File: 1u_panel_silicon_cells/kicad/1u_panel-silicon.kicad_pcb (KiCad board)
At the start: 2 copper layers, 83 x 100 mm, 148 parts, among them J1 MMS-104-01-[F/L]-SH, J2 2-1734592-0, Q1 DMP3050LVT-7, Q2 DMP2240UDM-7, U1 TCAN330GDCNT, U10 TPS63060DSCR, U11 TMP101NA/3KSLOTTED, U12 LTC4412, U13 LTC4411, U14 LTC4411, U15 LTC4411, U16 LTC4411, U2 TMP101NA/3KSLOTTED, U3 LT1618EMSTRPBF, U4 INA226, U5 LTC4411, U6 LTC4411, U7 STM32F091CCT7, U8 LTC4411, U9 LTC4411, X1 ECS-160-10-36Q-ES-TR

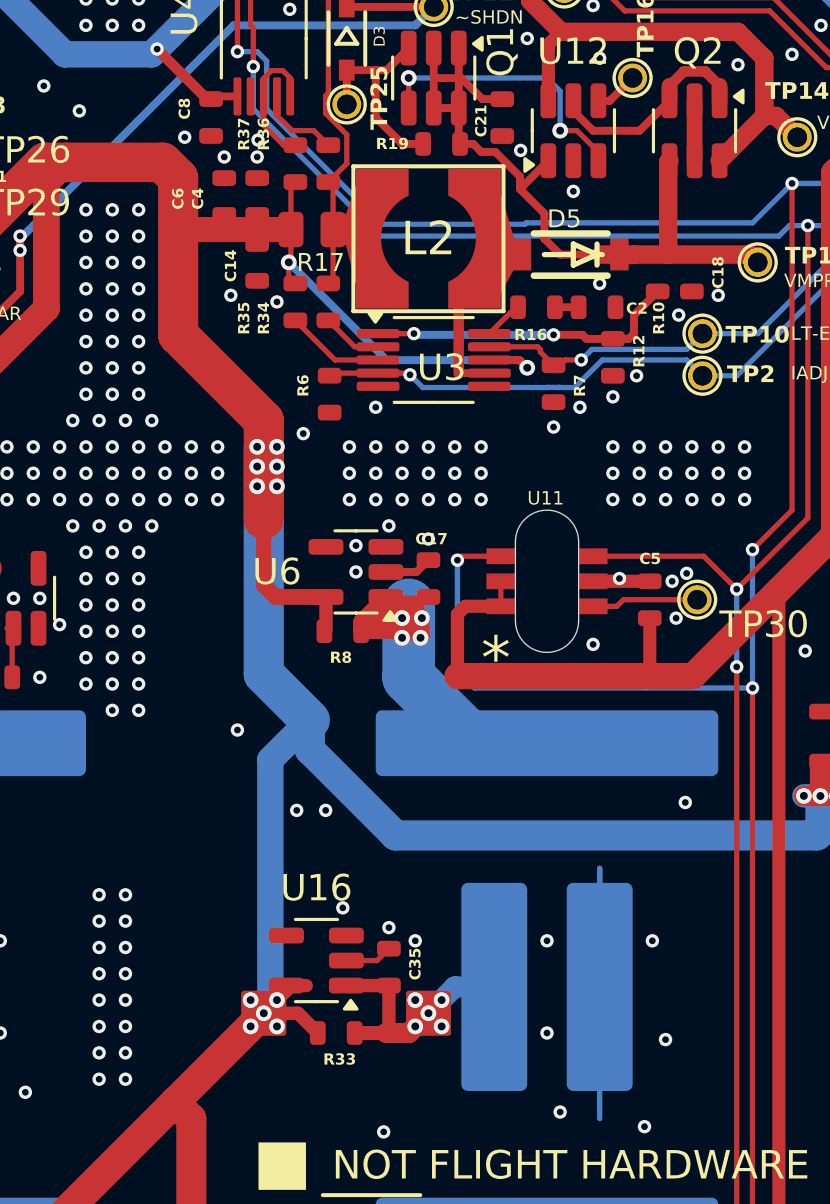
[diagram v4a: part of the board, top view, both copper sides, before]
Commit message: Updated all PN/DS/DPN/MPN/etc. for silicon solar module components
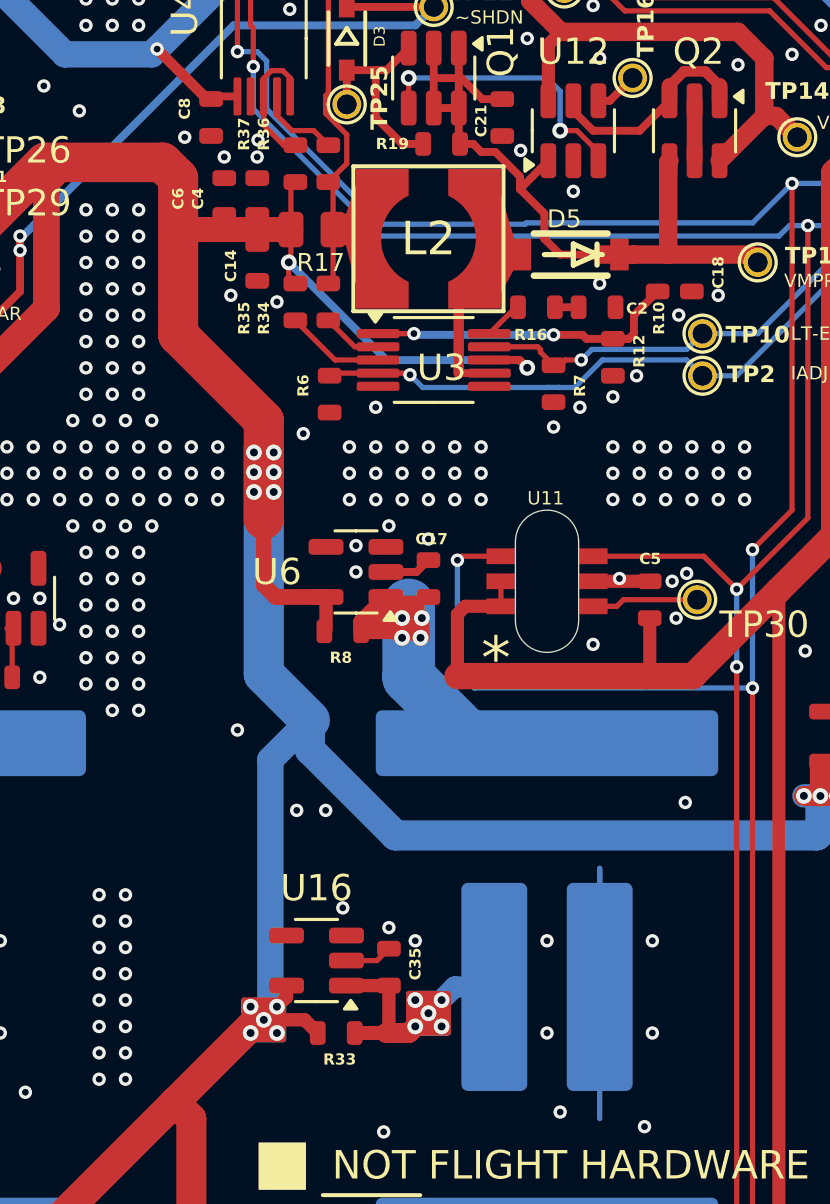
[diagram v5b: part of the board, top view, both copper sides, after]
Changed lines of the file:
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@@
 	)
 	(gr_rect
-		(start 137 105.25)
-		(end 138.5 106.75)
+		(start 137 105.5)
+		(end 138.5 107)
 		(stroke
 			(width 0.2)
@@
 	)
 	(gr_rect
-		(start 137 105.25)
-		(end 138.5 106.75)
+		(start 137 105.5)
+		(end 138.5 107)
 		(stroke
 			(width 0.2)
@@
 	)
 	(segment
-		(start 139.3625 104.95)
-		(end 138.8 104.95)
-		(width 0.508)
-		(layer "F.Cu")
-		(net 2)
-	)
-	(segment
 		(start 135 110)
 		(end 134.375 109.375)
@@
 	)
 	(segment
+		(start 134.5 80.25)
+		(end 137.75 83.5)
+		(width 1.524)
+		(layer "F.Cu")
+		(net 2)
+	)
+	(segment
 		(start 129.287611 114.462389)
 		(end 129.287611 117.962389)
@@
 	)
 	(segment
-		(start 134.5 80.25)
-		(end 137.75 83.5)
-		(width 1.524)
+		(start 138.6125 104.95)
+		(end 138.6125 105.3875)
+		(width 0.508)
 		(layer "F.Cu")
 		(net 2)
 	)
 	(segment
-		(start 137.75 106)
-		(end 139.05 106)
+		(start 174.125 103.375)
+		(end 174.125 101.5)
 		(width 0.508)
 		(layer "F.Cu")
@@
 	)
 	(segment
-		(start 174.125 103.375)
-		(end 174.125 101.5)
+		(start 139.3 106.25)
+		(end 139.8 106.75)
 		(width 0.508)
 		(layer "F.Cu")
@@
 	)
 	(segment
-		(start 134.5 76)
-		(end 134.5 80.25)
+		(start 133.9011 73.7036)
+		(end 134.5 74.3025)
+		(width 1.524)
+		(layer "F.Cu")
+		(net 2)
+	)
+	(segment
+		(start 137.75 83.5)
+		(end 137.75 87.25)
 		(width 1.524)
 		(layer "F.Cu")
@@
 	)
 	(segment
-		(start 137.75 83.5)
-		(end 137.75 87.25)
-		(width 1.524)
+		(start 158.25 97.75)
+		(end 159.8 97.75)
+		(width 0.762)
 		(layer "F.Cu")
 		(net 2)
 	)
 	(segment
-		(start 158.25 97.75)
-		(end 159.8 97.75)
-		(width 0.762)
+		(start 134.5 74.3025)
+		(end 134.5 80.25)
+		(width 1.524)
 		(layer "F.Cu")
 		(net 2)
@@
 	)
 	(segment
-		(start 134.5 74.3025)
-		(end 134.5 76)
-		(width 1.524)
-		(layer "F.Cu")
-		(net 2)
-	)
-	(segment
 		(start 138.6125 121.6125)
 		(end 135 118)
@@
 	)
 	(segment
-		(start 139.05 106)
-		(end 139.8 106.75)
-		(width 0.508)
-		(layer "F.Cu")
-		(net 2)
-	)
-	(segment
 		(start 134.753898 76.253898)
 		(end 138.780425 76.253898)
@@
 	)
 	(segment
-		(start 138.8 104.95)
-		(end 137.75 106)
-		(width 0.508)
-		(layer "F.Cu")
-		(net 2)
-	)
-	(segment
 		(start 138.780425 76.253898)
 		(end 138.780425 77.418475)
@@
 	)
 	(segment
+		(start 138.6125 105.3875)
+		(end 137.75 106.25)
+		(width 0.508)
+		(layer "F.Cu")
+		(net 2)
+	)
+	(segment
 		(start 125.3011 76.5036)
 		(end 125.3011 76.3786)
@@
 	)
 	(segment
-		(start 141.75 121.6125)
-		(end 138.6125 121.6125)
-		(width 1.143)
+		(start 137.75 106.25)
+		(end 139.3 106.25)
+		(width 0.508)
 		(layer "F.Cu")
 		(net 2)
 	)
 	(segment
-		(start 133.9011 73.7036)
-		(end 134.5 74.3025)
-		(width 1.524)
+		(start 141.75 121.6125)
+		(end 138.6125 121.6125)
+		(width 1.143)
 		(layer "F.Cu")
 		(net 2)
@@
 	)
 	(via
-		(at 137.5 86)
+		(at 137.377208 86.214756)
 		(size 0.6)
 		(drill 0.3)
@@
 	)
 	(via
-		(at 137.25 106.5)
+		(at 137.25 106.75)
 		(size 0.6)
 		(drill 0.3)
@@
 	)
 	(via
-		(at 137.5 84.5)
+		(at 137.377208 84.714756)
 		(size 0.6)
 		(drill 0.3)
@@
 	)
 	(via
-		(at 137.75 106)
+		(at 137.75 106.25)
 		(size 0.6)
 		(drill 0.3)
@@
 	)
 	(via
-		(at 138.25 106.5)
+		(at 138.25 106.75)
 		(size 0.6)
 		(drill 0.3)
@@
 	)
 	(via
-		(at 138.25 105.5)
+		(at 138.25 105.75)
 		(size 0.6)
 		(drill 0.3)
@@
 	)
 	(via
-		(at 137.25 105.5)
+		(at 137.25 105.75)
 		(size 0.6)
 		(drill 0.3)
@@
 	)
 	(via
-		(at 138.25 86)
+		(at 138.127208 86.214756)
 		(size 0.6)
 		(drill 0.3)
@@
 	)
 	(via
-		(at 138.25 85.25)
+		(at 138.127208 85.464756)
 		(size 0.6)
 		(drill 0.3)
@@
 	)
 	(via
-		(at 137.5 85.25)
+		(at 137.377208 85.464756)
 		(size 0.6)
 		(drill 0.3)
@@
 	)
 	(via
-		(at 138.25 84.5)
+		(at 138.127208 84.714756)
 		(size 0.6)
 		(drill 0.3)
@@
 	)
 	(segment
+		(start 139.5 94.875)
+		(end 138 96.375)
+		(width 1)
+		(layer "B.Cu")
+		(net 2)
+	)
+	(segment
 		(start 158.877205 99.122795)
 		(end 158.75 99.25)
@@
 	)
 	(segment
+		(start 138 96.375)
+		(end 138 106)
+		(width 1)
+		(layer "B.Cu")
+		(net 2)
+	)
+	(segment
 		(start 171 97.75)
 		(end 174.75 101.5)
@@
 	)
 	(segment
-		(start 138 105.75)
-		(end 137.75 106)
+		(start 138 106)
+		(end 137.75 106.25)
 		(width 1)
 		(layer "B.Cu")
@@
 	)
 	(segment
-		(start 138 96.375)
-		(end 138 105.75)
-		(width 1)
-		(layer "B.Cu")
-		(net 2)
-	)
-	(segment
 		(start 142.75 99.25)
 		(end 139.5 96)
@@
 	)
 	(segment
-		(start 139.5 94.875)
-		(end 138 96.375)
-		(width 1)
-		(layer "B.Cu")
-		(net 2)
-	)
-	(segment
 		(start 170.2947 80.31)
 		(end 173.75 76.8547)
@@
 	)
 	(via
-		(at 153 107)
+		(at 152.5 106.75)
 		(size 0.508)
 		(drill 0.254)

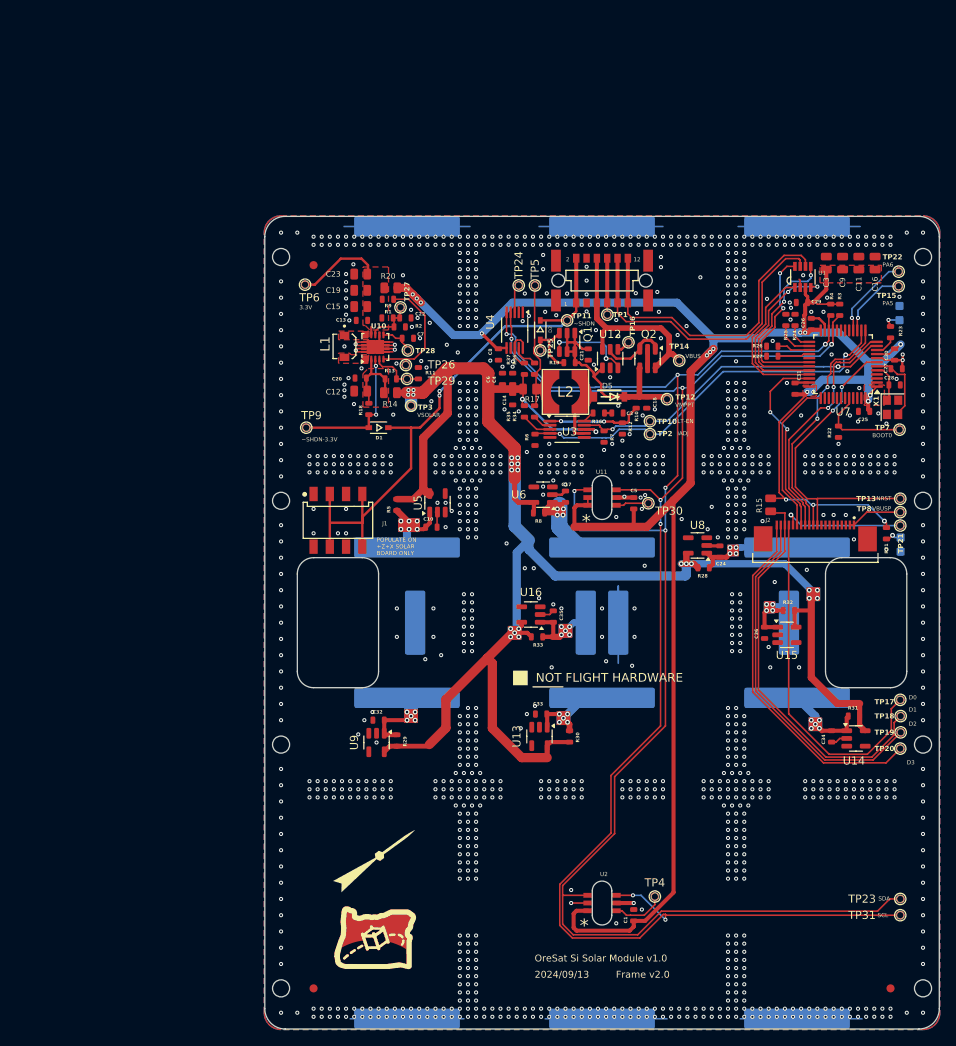
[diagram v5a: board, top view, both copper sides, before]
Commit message: finished DR changes for silicon solar module
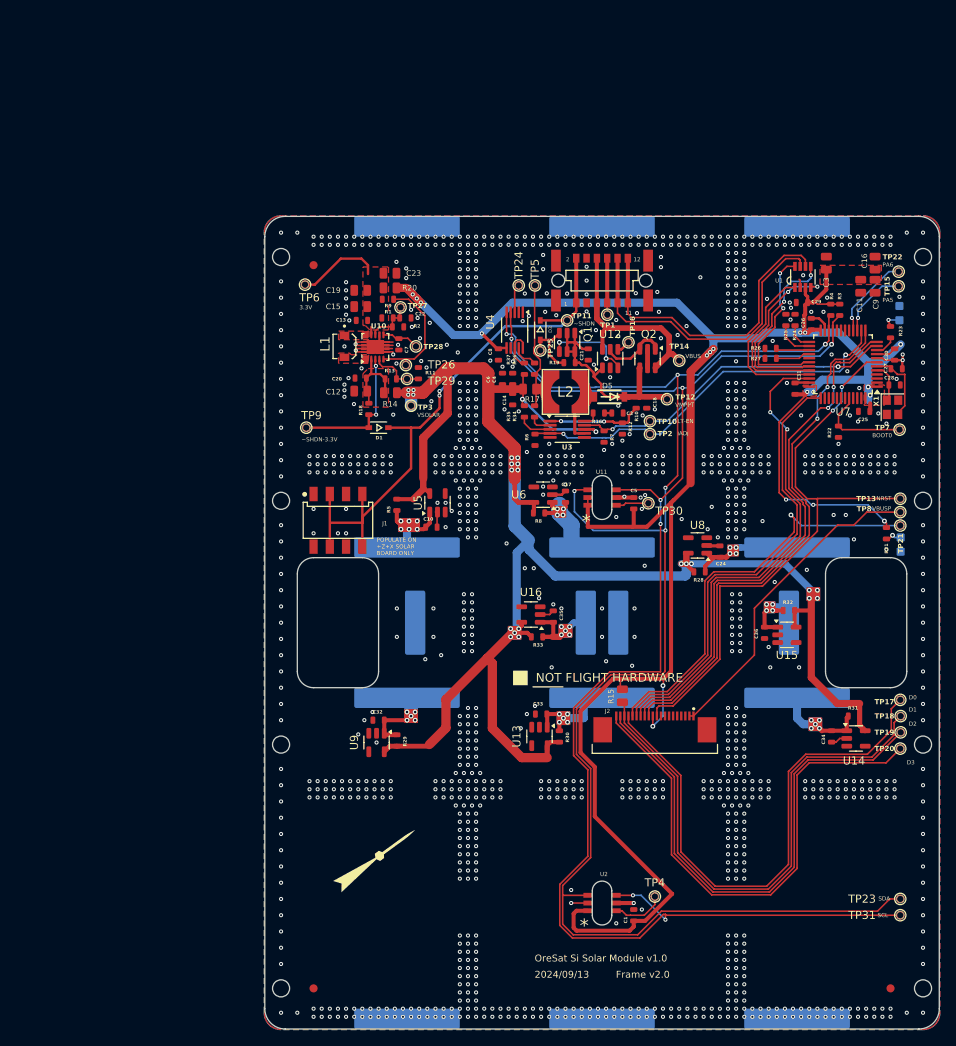
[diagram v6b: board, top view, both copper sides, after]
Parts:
- removed REF**: logo-small, oresat-graphics:logo-small
- moved J2 30.7 mm to (155.0, 118.2)
- moved R15 29.8 mm to (151.0, 114.0)
- moved C9 4.91 mm to (182.1, 63.6), turned to -90 degrees
- moved C23 3.60 mm to (122.4, 62.0), turned to 0 degrees
- moved C11 2.85 mm to (180.3, 63.6), turned to -90 degrees
- moved C7 1.33 mm to (123.5, 70.7), turned to -90 degrees
- moved R30 1.25 mm to (143.2, 119.0)
- moved TP28 1.12 mm to (125.6, 71.0)
- moved R28 0.71 mm to (160.5, 98.8)
- moved R26 0.34 mm to (169.2, 71.2)
- moved R27 0.34 mm to (169.2, 72.5)
- moved R2 0.20 mm to (123.4, 68.6)
- moved R20 0.10 mm to (122.4, 63.8)
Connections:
- R23 pad 1: Net-(D6-PadA) -> Net-(D6-A)
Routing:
- net GND: track 138.2 -> 34.4 mm, vias 1222 -> 1221
- net Net-(J2-SWO): track 15.3 -> 51.4 mm
- net /1u_panel-microcontroller/PA3/USART2_RX: track 29.6 -> 65.1 mm
- net /1u_panel-microcontroller/PA2/USART2_TX: track 29.9 -> 65.5 mm
- net /1u_panel-microcontroller/SWDIO: track 23.6 -> 59.1 mm
- net /1u_panel-microcontroller/SWCLK: track 19.3 -> 54.8 mm
- net /1u_panel-microcontroller/NRESET: track 37.0 -> 72.3 mm
- net Net-(J2-VBUSP-Pad1): track 6.86 -> 39.7 mm
- net Net-(J2-DEBUG-0): track 43.4 -> 65.9 mm
- net Net-(J2-DEBUG-3): track 44.3 -> 64.3 mm
- net Net-(J2-DEBUG-2): track 44.5 -> 64.4 mm
- net Net-(J2-DEBUG-1): track 48.6 -> 66.7 mm
- net 3.3V: track 261.6 -> 272.9 mm, vias 17 -> 19
- net Net-(D7-A1): track 19.1 -> 13.6 mm
- net SCL: track 182.6 -> 187.7 mm
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
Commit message: final changes for silicon solar module
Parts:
- X1: footprint Crystal:Crystal_SMD_2520-4Pin_2.5x2.0mm -> oresat-misc:ECS-160-10-36Q-ES-TR
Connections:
- U3 pad 6: (no net) -> unconnected-(U3-NC-Pad6)
- X1 pad 4: (no net) -> GND
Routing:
- net GND: track 34.4 -> 35.2 mm
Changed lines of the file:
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@@
 	(net 101 "Net-(U3-ISN)")
 	(net 102 "Net-(U3-ISP)")
+	(net 103 "unconnected-(U3-NC-Pad6)")
 	(footprint "oresat-misc:TestPoint-0.75mm-th"
 		(layer "F.Cu")
@@
 		)
 	)
-	(footprint "Crystal:Crystal_SMD_2520-4Pin_2.5x2.0mm"
+	(footprint "oresat-misc:ECS-160-10-36Q-ES-TR"
 		(layer "F.Cu")
 		(at 184.25 78.5 -90)
@@
 		(tags "SMD SMT crystal")
 		(property "Reference" "X1"
-			(at -0.75 2 -90)
+			(at 0 -2.2 90)
 			(layer "F.SilkS")
 			(effects
 				(font
-					(size 0.635 0.635)
-					(thickness 0.127)
-					(bold yes)
+					(size 1 1)
+					(thickness 0.15)
 				)
 			)
@@
 			)
 		)
-		(property "Footprint" "Crystal:Crystal_SMD_2520-4Pin_2.5x2.0mm"
+		(property "Footprint" "oresat-misc:ECS-160-10-36Q-ES-TR"
 			(at 0 0 -90)
 			(unlocked yes)
@@
 			)
 		)
-		(property "Description" "Three pin crystal, GND on pin 2"
+		(property "Description" "Four pin crystal, GND on pins 2 and 4"
 			(at 0 0 -90)
 			(unlocked yes)
@@
 		)
 		(pad "1" smd rect
-			(at -0.875 0.7 270)
-			(size 1.15 1)
+			(at -0.85 0.65 270)
+			(size 1.2 1)
 			(layers "F.Cu" "F.Paste" "F.Mask")
 			(net 95 "/1u_panel-microcontroller/OSC_IN")
@@
 		)
 		(pad "2" smd rect
-			(at 0.875 0.7 270)
-			(size 1.15 1)
+			(at 0.85 0.65 270)
+			(size 1.2 1)
 			(layers "F.Cu" "F.Paste" "F.Mask")
 			(net 7 "GND")
@@
 		)
 		(pad "3" smd rect
-			(at 0.875 -0.7 270)
-			(size 1.15 1)
+			(at 0.85 -0.65 270)
+			(size 1.2 1)
 			(layers "F.Cu" "F.Paste" "F.Mask")
 			(net 94 "/1u_panel-microcontroller/OSC_OUT")
@@
 		)
 		(pad "4" smd rect
-			(at -0.875 -0.7 270)
-			(size 1.15 1)
+			(at -0.85 -0.65 270)
+			(size 1.2 1)
 			(layers "F.Cu" "F.Paste" "F.Mask")
+			(net 7 "GND")
+			(pinfunction "4")
+			(pintype "passive")
 		)
 		(model "${KICAD8_3DMODEL_DIR}/Crystal.3dshapes/Crystal_SMD_2520-4Pin_2.5x2.0mm.wrl"
@@
 			(layers "F.Cu" "F.Paste" "F.Mask")
 			(roundrect_rratio 0.25)
+			(net 103 "unconnected-(U3-NC-Pad6)")
+			(pinfunction "NC")
+			(pintype "passive+no_connect")
 		)
 		(pad "7" smd roundrect
@@
 	)
 	(segment
+		(start 124.1 68.027936)
+		(end 124.119351 68.008585)
+		(width 0.2)
+		(layer "F.Cu")
+		(net 7)
+	)
+	(segment
 		(start 163 95.55)
 		(end 161.4375 95.55)
@@
 	)
 	(segment
+		(start 124.1 68.6)
+		(end 124.1 68.027936)
+		(width 0.2)
+		(layer "F.Cu")
+		(net 7)
+	)
+	(segment
 		(start 142.3875 89.25)
 		(end 143.55 89.25)
@@
 	)
 	(segment
+		(start 124.119351 68.008585)
+		(end 124.263968 67.863968)
+		(width 0.2)
+		(layer "F.Cu")
+		(net 7)
+	)
+	(segment
 		(start 142.05 104)
 		(end 142.5 103.55)
@@
 	)
 	(segment
-		(start 184.95 79.125)
-		(end 185.7524 78.3226)
+		(start 184.44975 73.44975)
+		(end 182.325 73.44975)
 		(width 0.2)
 		(layer "F.Cu")
@@
 	)
 	(segment
-		(start 185.7524 74.4548)
-		(end 185.75 74.4524)
+		(start 185.129164 74.4524)
+		(end 184.8 74.123236)
 		(width 0.2)
 		(layer "F.Cu")
@@
 	)
 	(segment
-		(start 185.75 74.4524)
-		(end 184.8529 74.4524)
+		(start 184.8 73.8)
+		(end 184.44975 73.44975)
+		(width 0.2)
+		(layer "F.Cu")
+		(net 94)
+	)
+	(segment
+		(start 184.8 74.123236)
+		(end 184.8 73.8)
 		(width 0.2)
 		(layer "F.Cu")
@@
 	)
 	(segment
-		(start 183.85025 73.44975)
-		(end 182.325 73.44975)
+		(start 185.7524 74.4548)
+		(end 185.75 74.4524)
 		(width 0.2)
 		(layer "F.Cu")
@@
 	)
 	(segment
-		(start 184.8529 74.4524)
-		(end 183.85025 73.44975)
+		(start 185.75 74.4524)
+		(end 185.129164 74.4524)
+		(width 0.2)
+		(layer "F.Cu")
+		(net 94)
+	)
+	(segment
+		(start 184.95 79.125)
+		(end 185.7524 78.3226)
 		(width 0.2)
 		(layer "F.Cu")
@@
 		(filled_areas_thickness no)
 		(fill yes
-			(thermal_gap 0.127)
+			(thermal_gap 0.1524)
 			(thermal_bridge_width 0.2)
 			(smoothing chamfer)
-			(radius 0.127)
+			(radius 0.1524)
 		)
 		(polygon
